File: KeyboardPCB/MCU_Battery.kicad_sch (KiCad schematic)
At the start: 11 parts

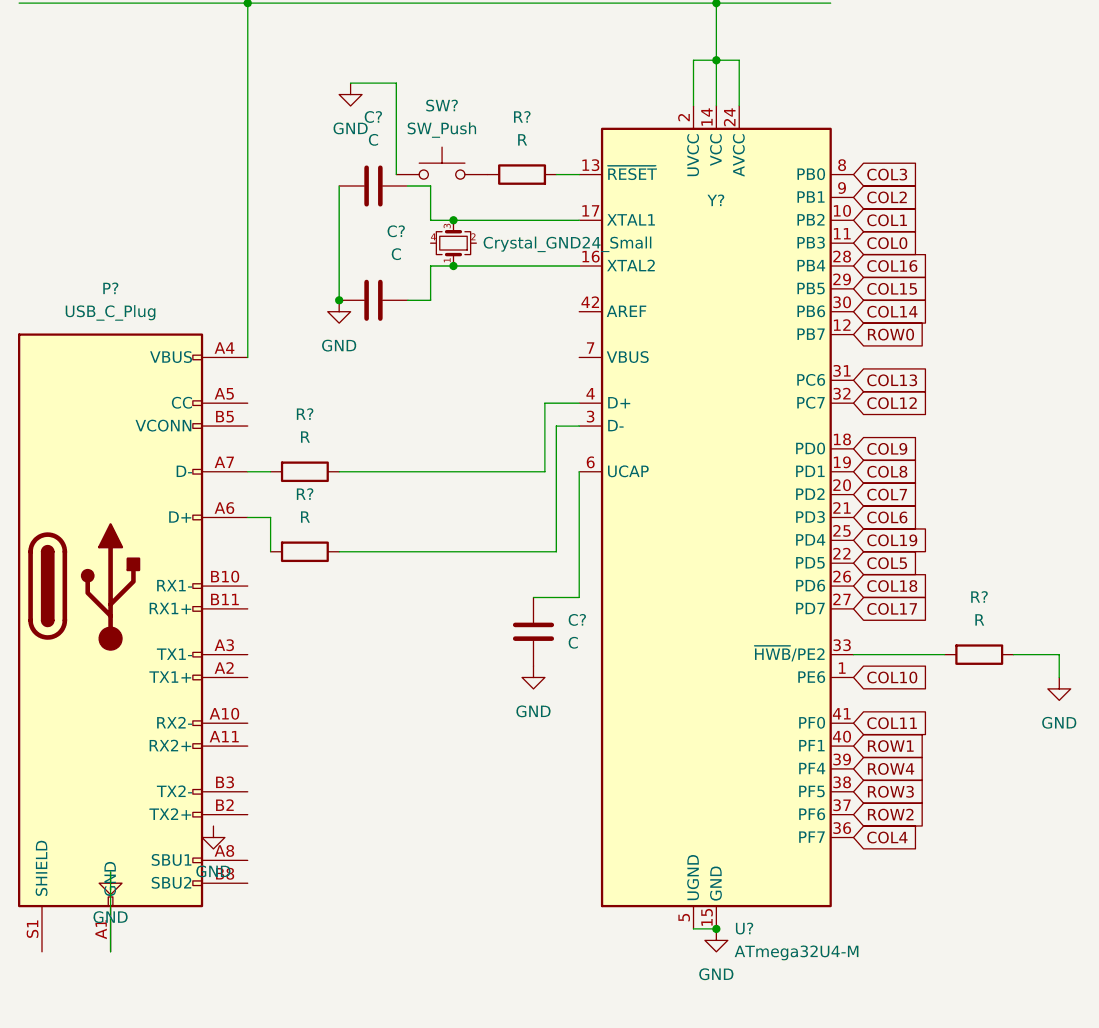
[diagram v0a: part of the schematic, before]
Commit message: set up for key array
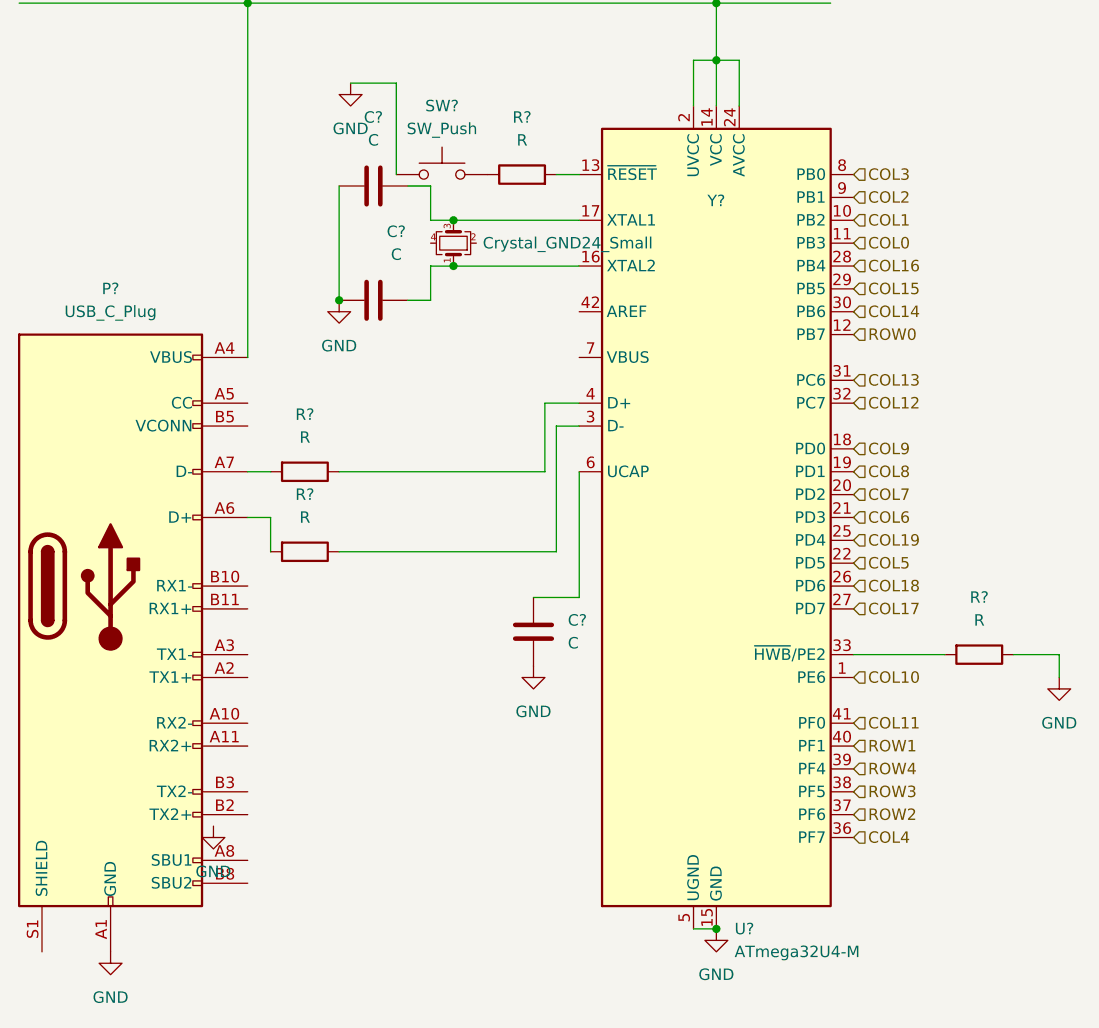
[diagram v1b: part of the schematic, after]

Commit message: Worked on battery charging system
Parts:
- removed R? (x2): R, symbol Device:R
- added C? (x2): C, symbol Device:C
- added P?: USB_C_Plug, symbol Connector:USB_C_Plug
- added R? (x2): R, symbol Device:R
- added U?: KA78M05_TO252, Package_TO_SOT_SMD:TO-252-2, symbol Regulator_Linear:KA78M05_TO252
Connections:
- net GND: now also Y?.2, Y?.4, C?.2, C?.2, P?.A1 (GND), P?.A12 (GND), P?.B1 (GND), P?.B12 (GND), U?.2 (GND)
- net at U?.3 (D-): now also R?.1
- net at P?.A6 (D+): now also R?.2
- net at P?.A4 (VBUS), P?.A9 (VBUS), P?.B4 (VBUS)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: now also C?.1, U?.1 (VI)
- net at U?.4 (D+): now also R?.1
- net at P?.A7 (D-): now also R?.2
- new net: P?.A4 (VBUS), P?.A9 (VBUS), P?.B4 (VBUS), P?.B9 (VBUS)
- new net: C?.1, U?.3 (VO)
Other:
- moved on the sheet: C?, Y?

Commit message: added some diodes
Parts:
- removed C? (x2): C, symbol Device:C
- removed U?: KA78M05_TO252, Package_TO_SOT_SMD:TO-252-2, symbol Regulator_Linear:KA78M05_TO252
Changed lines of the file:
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@@
   (junction (at 102.87 128.27) (diameter 0) (color 0 0 0 0)
   )
-  (junction (at 102.87 25.4) (diameter 0) (color 0 0 0 0)
-  )
-  (junction (at 142.24 25.4) (diameter 0) (color 0 0 0 0)
-  )
   (junction (at 60.96 58.42) (diameter 0) (color 0 0 0 0)
   )
@@
   (junction (at 74.93 49.53) (diameter 0) (color 0 0 0 0)
   )
-  (junction (at 152.4 33.02) (diameter 0) (color 0 0 0 0)
-  )
   (junction (at 60.96 62.23) (diameter 0) (color 0 0 0 0)
   )
@@
     (stroke (width 0) (type default) (color 0 0 0 0))
   )
-  (wire (pts (xy 142.24 25.4) (xy 144.78 25.4))
-    (stroke (width 0) (type default) (color 0 0 0 0))
-  )
   (wire (pts (xy 74.93 54.61) (xy 87.63 54.61))
     (stroke (width 0) (type default) (color 0 0 0 0))
@@
     (stroke (width 0) (type default) (color 0 0 0 0))
   )
-  (wire (pts (xy 142.24 33.02) (xy 152.4 33.02))
-    (stroke (width 0) (type default) (color 0 0 0 0))
-  )
   (wire (pts (xy 82.55 114.3) (xy 82.55 128.27))
     (stroke (width 0) (type default) (color 0 0 0 0))
@@
     (stroke (width 0) (type default) (color 0 0 0 0))
   )
-  (wire (pts (xy 152.4 34.29) (xy 152.4 33.02))
-    (stroke (width 0) (type default) (color 0 0 0 0))
-  )
   (wire (pts (xy 60.96 58.42) (xy 60.96 45.72))
     (stroke (width 0) (type default) (color 0 0 0 0))
@@
     (stroke (width 0) (type default) (color 0 0 0 0))
   )
-  (wire (pts (xy 162.56 25.4) (xy 160.02 25.4))
-    (stroke (width 0) (type default) (color 0 0 0 0))
-  )
-  (wire (pts (xy 152.4 33.02) (xy 162.56 33.02))
-    (stroke (width 0) (type default) (color 0 0 0 0))
-  )
   (wire (pts (xy 77.47 62.23) (xy 77.47 52.07))
     (stroke (width 0) (type default) (color 0 0 0 0))
@@
   )
   (wire (pts (xy 100.33 31.75) (xy 102.87 31.75))
-    (stroke (width 0) (type default) (color 0 0 0 0))
-  )
-  (wire (pts (xy 102.87 25.4) (xy 142.24 25.4))
     (stroke (width 0) (type default) (color 0 0 0 0))
   )
@@
     (pin "S1")
   )
-  (symbol (lib_id "Device:C") (at 142.24 29.21 0) (unit 1)
-    (in_bom yes) (on_board yes)
-    (property "Reference" "C?" (id 0) (at 135.89 27.94 0)
-      (effects (font (size 1.27 1.27)) (justify left))
-    )
-    (property "Value" "C" (id 1) (at 135.89 30.48 0)
-      (effects (font (size 1.27 1.27)) (justify left))
-    )
-    (property "Footprint" "" (id 2) (at 143.2052 33.02 0)
-      (effects (font (size 1.27 1.27)) hide)
-    )
-    (property "Datasheet" "~" (id 3) (at 142.24 29.21 0)
-      (effects (font (size 1.27 1.27)) hide)
-    )
-    (pin "1")
-    (pin "2")
-  )
   (symbol (lib_id "Device:R") (at 81.28 44.45 90) (unit 1)
     (in_bom yes) (on_board yes) (fields_autoplaced)
@@
     (pin "1")
   )
-  (symbol (lib_id "Regulator_Linear:KA78M05_TO252") (at 152.4 25.4 0) (unit 1)
-    (in_bom yes) (on_board yes) (fields_autoplaced)
-    (property "Reference" "U?" (id 0) (at 152.4 17.78 0))
-    (property "Value" "KA78M05_TO252" (id 1) (at 152.4 20.32 0))
-    (property "Footprint" "Package_TO_SOT_SMD:TO-252-2" (id 2) (at 152.4 19.685 0)
-      (effects (font (size 1.27 1.27) italic) hide)
-    )
-    (property "Datasheet" "https://www.onsemi.com/pub/Collateral/MC78M00-D.PDF" (id 3) (at 152.4 26.67 0)
-      (effects (font (size 1.27 1.27)) hide)
-    )
-    (pin "1")
-    (pin "2")
-    (pin "3")
-  )
   (symbol (lib_id "Device:C") (at 64.77 45.72 270) (unit 1)
     (in_bom yes) (on_board yes) (fields_autoplaced)
@@
     (pin "1")
   )
-  (symbol (lib_id "power:GND") (at 152.4 34.29 0) (unit 1)
-    (in_bom yes) (on_board yes) (fields_autoplaced)
-    (property "Reference" "#PWR?" (id 0) (at 152.4 40.64 0)
-      (effects (font (size 1.27 1.27)) hide)
-    )
-    (property "Value" "GND" (id 1) (at 152.4 39.37 0))
-    (property "Footprint" "" (id 2) (at 152.4 34.29 0)
-      (effects (font (size 1.27 1.27)) hide)
-    )
-    (property "Datasheet" "" (id 3) (at 152.4 34.29 0)
-      (effects (font (size 1.27 1.27)) hide)
-    )
-    (pin "1")
-  )
-  (symbol (lib_id "Device:C") (at 162.56 29.21 0) (unit 1)
-    (in_bom yes) (on_board yes) (fields_autoplaced)
-    (property "Reference" "C?" (id 0) (at 166.37 27.9399 0)
-      (effects (font (size 1.27 1.27)) (justify left))
-    )
-    (property "Value" "C" (id 1) (at 166.37 30.4799 0)
-      (effects (font (size 1.27 1.27)) (justify left))
-    )
-    (property "Footprint" "" (id 2) (at 163.5252 33.02 0)
-      (effects (font (size 1.27 1.27)) hide)
-    )
-    (property "Datasheet" "~" (id 3) (at 162.56 29.21 0)
-      (effects (font (size 1.27 1.27)) hide)
-    )
-    (pin "1")
-    (pin "2")
-  )
   (symbol (lib_id "power:GND") (at 60.96 64.77 0) (unit 1)

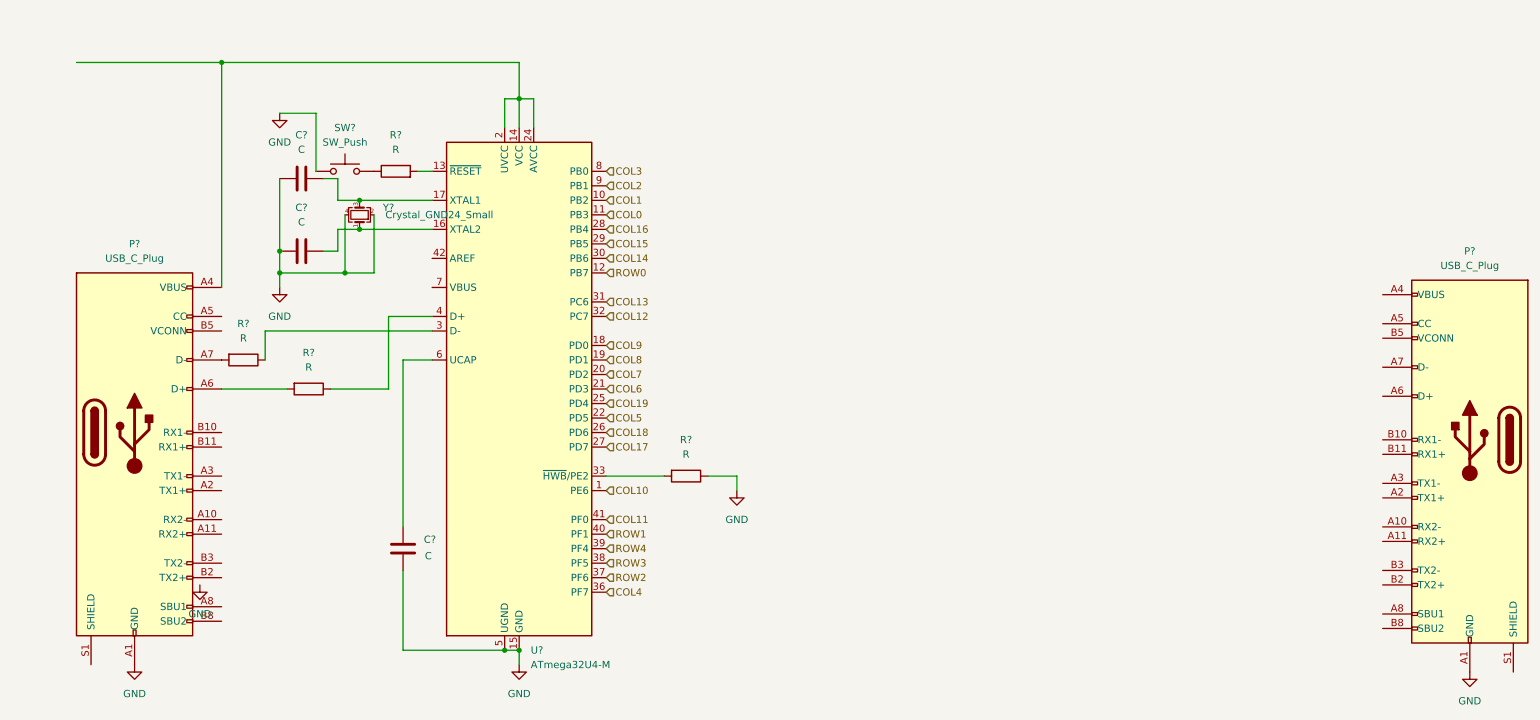
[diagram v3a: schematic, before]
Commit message: Added a Battery Charging circuit
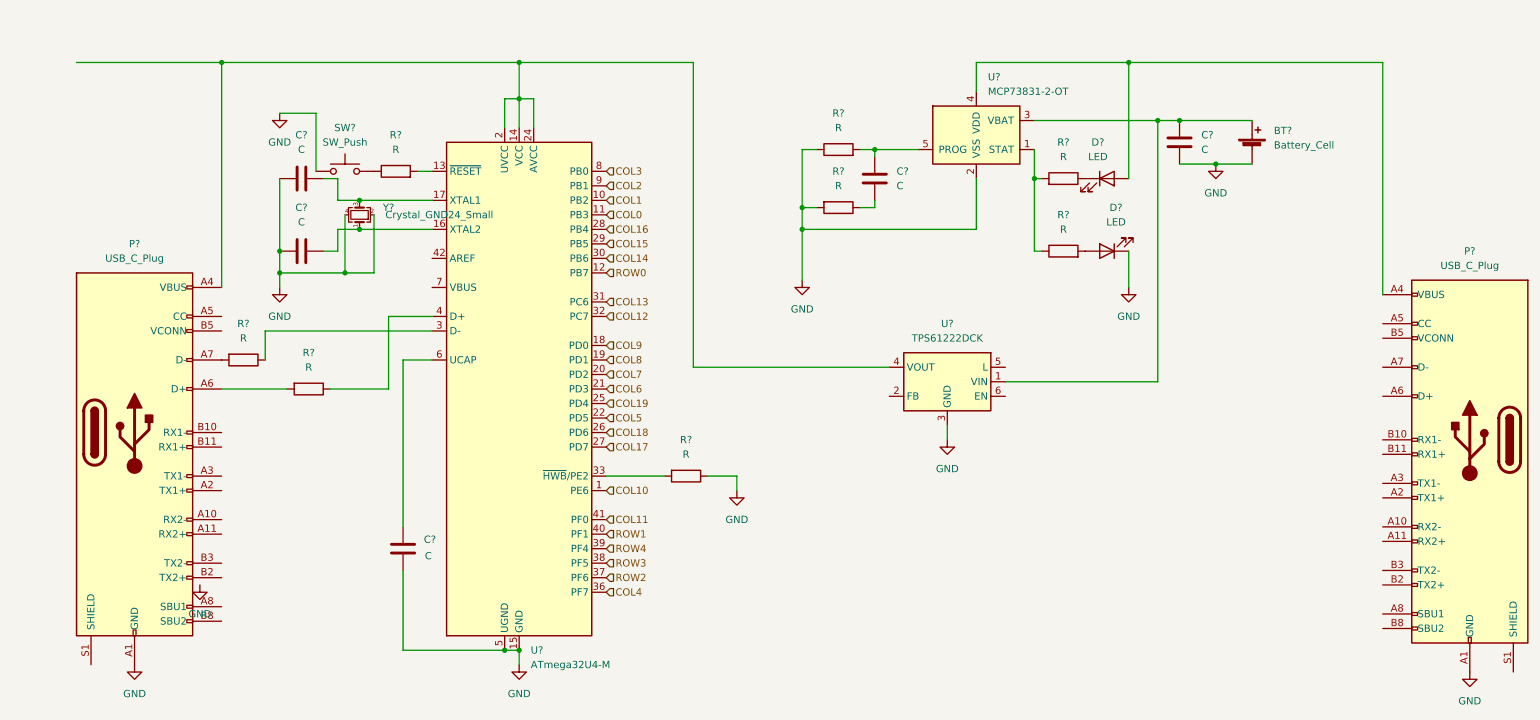
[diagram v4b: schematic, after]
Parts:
- added BT?: Battery_Cell, symbol Device:Battery_Cell
- added C? (x2): C, symbol Device:C
- added D? (x2): LED, symbol Device:LED
- added R? (x4): R, symbol Device:R
- added U?: TPS61222DCK, Package_TO_SOT_SMD:Texas_R-PDSO-G6, symbol Regulator_Switching:TPS61222DCK
- added U?: MCP73831-2-OT, Package_TO_SOT_SMD:SOT-23-5, symbol Battery_Management:MCP73831-2-OT
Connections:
- net GND: now also BT?.2 (-), C?.2, D?.1 (K), R?.1, R?.2, U?.2 (VSS), U?.3 (GND)
- net at P?.A4 (VBUS), P?.A9 (VBUS), P?.B4 (VBUS)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: now also D?.2 (A), U?.4 (VDD)
- net at P?.A4 (VBUS), P?.A9 (VBUS), P?.B4 (VBUS)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: now also U?.4 (VOUT)
- new net: C?.2, R?.1
- new net: D?.1 (K), R?.1
- new net: R?.1, R?.2, U?.1 (STAT)
- new net: C?.1, R?.2, U?.5 (PROG)
- new net: BT?.1 (+), C?.1, U?.1 (VIN), U?.3 (VBAT)
- new net: D?.2 (A), R?.2

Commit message: reorganised the schematic
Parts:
- removed P? (x2): USB_C_Plug, symbol Connector:USB_C_Plug
- removed R? (x2): R, symbol Device:R
- added L?: L, symbol Device:L
- added R? (x2): R, symbol Device:R
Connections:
- net VBUSIN: now reaches D?.2 (A), U?.4 (VDD)
- net VBUSOUT: now reaches U?.14 (VCC), U?.2 (UVCC), U?.24 (AVCC), U?.34 (VCC), U?.4 (VOUT), U?.44 (AVCC)
- net VBUSOUT: now also U?.2 (FB)
- net at U?.3 (D-): now also R?.2
- net at U?.4 (D+): now also R?.2
- net at BT?.1 (+), C?.1, U?.1 (VIN)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: now also U?.6 (EN), L?.2
- net at U?.5 (L): now also L?.1
- new net USBUFPD+: R?.1
- new net USBUFPD-: R?.1
